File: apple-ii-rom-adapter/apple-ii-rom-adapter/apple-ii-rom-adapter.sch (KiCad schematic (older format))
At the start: 11 parts, among them J1 ROMSEL, J2 9316 insert, J3 74LS138 insert, U1 28C256, U2 74LS00, U3 74LS138

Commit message: Incremental update! Maybe this'll work? :-)
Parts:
- C1, C2, C3: footprint Capacitor_THT:CP_Radial_D6.3mm_P2.50mm -> Capacitor_THT:C_Disc_D5.0mm_W2.5mm_P5.00mm
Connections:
- net VCC: now also R2.1
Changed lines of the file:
@@
 F 0 "C1" H 6442 5646 50  0000 L CNN
 F 1 "0.1uF" H 6442 5555 50  0000 L CNN
-F 2 "Capacitor_THT:CP_Radial_D6.3mm_P2.50mm" H 6350 5600 50  0001 C CNN
+F 2 "Capacitor_THT:C_Disc_D5.0mm_W2.5mm_P5.00mm" H 6350 5600 50  0001 C CNN
 F 3 "~" H 6350 5600 50  0001 C CNN
 	1    6350 5600
@@
 F 0 "C2" H 7092 5646 50  0000 L CNN
 F 1 "0.1uF" H 7092 5555 50  0000 L CNN
-F 2 "Capacitor_THT:CP_Radial_D6.3mm_P2.50mm" H 7000 5600 50  0001 C CNN
+F 2 "Capacitor_THT:C_Disc_D5.0mm_W2.5mm_P5.00mm" H 7000 5600 50  0001 C CNN
 F 3 "~" H 7000 5600 50  0001 C CNN
 	1    7000 5600
@@
 F 0 "C3" H 7692 5646 50  0000 L CNN
 F 1 "0.1uF" H 7692 5555 50  0000 L CNN
-F 2 "Capacitor_THT:CP_Radial_D6.3mm_P2.50mm" H 7600 5600 50  0001 C CNN
+F 2 "Capacitor_THT:C_Disc_D5.0mm_W2.5mm_P5.00mm" H 7600 5600 50  0001 C CNN
 F 3 "~" H 7600 5600 50  0001 C CNN
 	1    7600 5600
@@
 $EndComp
 $Comp
-L power:GND #PWR?
+L power:GND #PWR0113
 U 1 1 60D30BF8
 P 6350 5700
-F 0 "#PWR?" H 6350 5450 50  0001 C CNN
+F 0 "#PWR0113" H 6350 5450 50  0001 C CNN
 F 1 "GND" H 6355 5527 50  0000 C CNN
 F 2 "" H 6350 5700 50  0001 C CNN
@@
 $EndComp
 $Comp
-L power:GND #PWR?
+L power:GND #PWR0114
 U 1 1 60D3171D
 P 7000 5700
-F 0 "#PWR?" H 7000 5450 50  0001 C CNN
+F 0 "#PWR0114" H 7000 5450 50  0001 C CNN
 F 1 "GND" H 7005 5527 50  0000 C CNN
 F 2 "" H 7000 5700 50  0001 C CNN
@@
 $EndComp
 $Comp
-L power:GND #PWR?
+L power:GND #PWR0115
 U 1 1 60D32097
 P 7600 5700
-F 0 "#PWR?" H 7600 5450 50  0001 C CNN
+F 0 "#PWR0115" H 7600 5450 50  0001 C CNN
 F 1 "GND" H 7605 5527 50  0000 C CNN
 F 2 "" H 7600 5700 50  0001 C CNN
@@
 $EndComp
 $Comp
-L power:VCC #PWR?
+L power:VCC #PWR0116
 U 1 1 60D32EAF
 P 6350 5500
-F 0 "#PWR?" H 6350 5350 50  0001 C CNN
+F 0 "#PWR0116" H 6350 5350 50  0001 C CNN
 F 1 "VCC" H 6365 5673 50  0000 C CNN
 F 2 "" H 6350 5500 50  0001 C CNN
@@
 $EndComp
 $Comp
-L power:VCC #PWR?
+L power:VCC #PWR0117
 U 1 1 60D33866
 P 7000 5500
-F 0 "#PWR?" H 7000 5350 50  0001 C CNN
+F 0 "#PWR0117" H 7000 5350 50  0001 C CNN
 F 1 "VCC" H 7015 5673 50  0000 C CNN
 F 2 "" H 7000 5500 50  0001 C CNN
@@
 $EndComp
 $Comp
-L power:VCC #PWR?
+L power:VCC #PWR0118
 U 1 1 60D346E6
 P 7600 5500
-F 0 "#PWR?" H 7600 5350 50  0001 C CNN
+F 0 "#PWR0118" H 7600 5350 50  0001 C CNN
 F 1 "VCC" H 7615 5673 50  0000 C CNN
 F 2 "" H 7600 5500 50  0001 C CNN
@@
 	1    0    0    -1
 $EndComp
+$Comp
+L power:VCC #PWR?
+U 1 1 60C6FC7E
+P 4250 5250
+F 0 "#PWR?" H 4250 5100 50  0001 C CNN
+F 1 "VCC" H 4265 5423 50  0000 C CNN
+F 2 "" H 4250 5250 50  0001 C CNN
+F 3 "" H 4250 5250 50  0001 C CNN
+	1    4250 5250
+	1    0    0    -1
+$EndComp

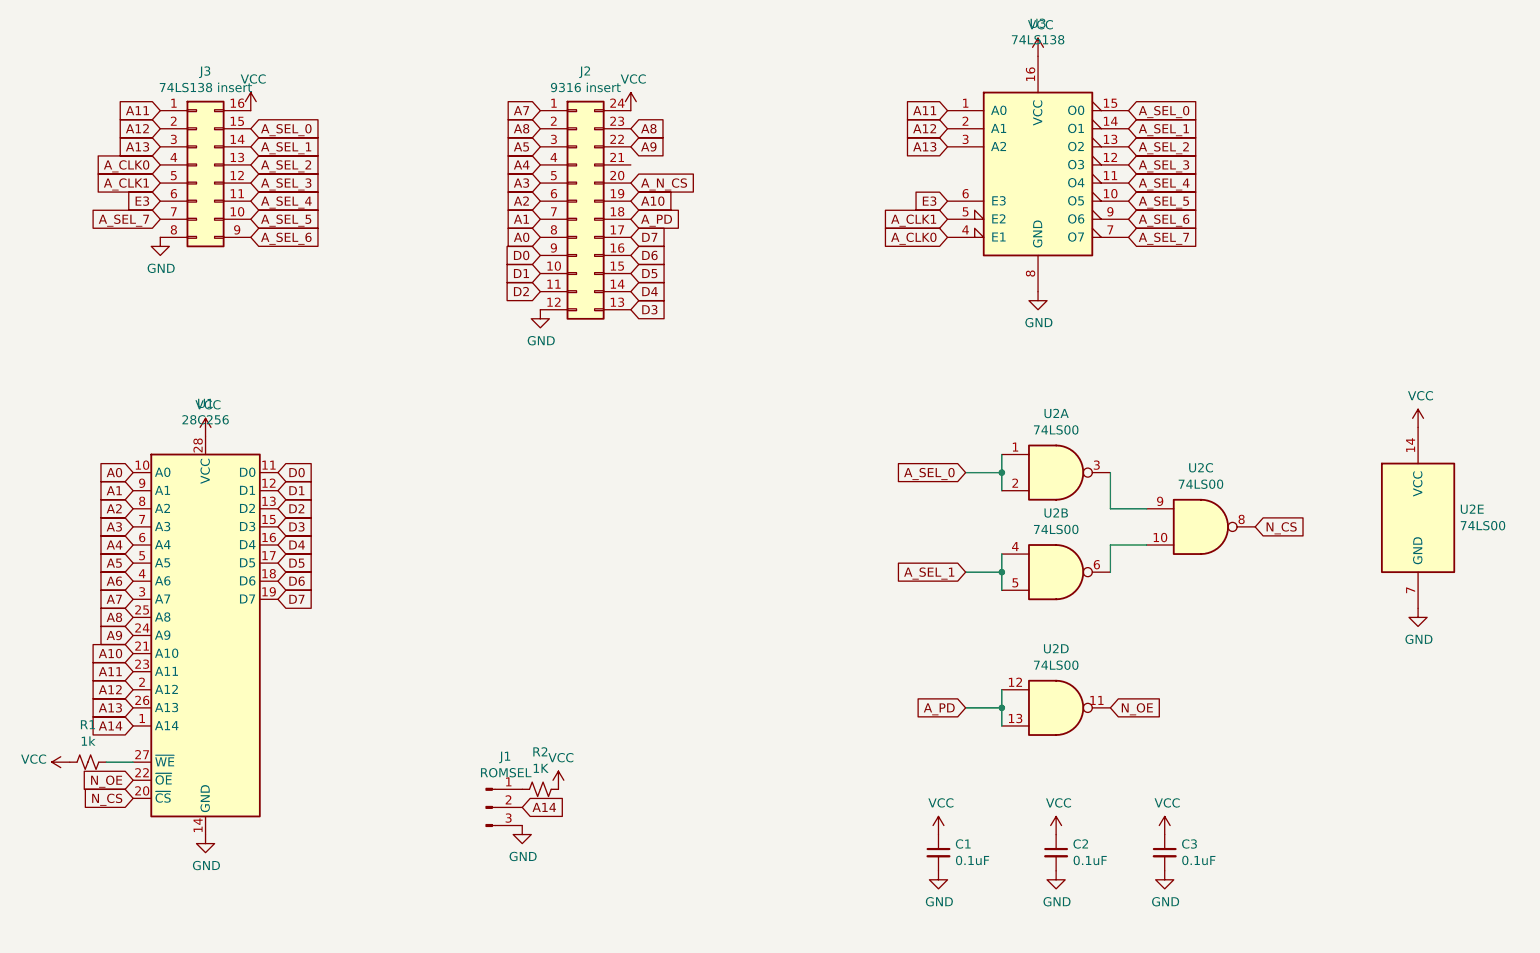
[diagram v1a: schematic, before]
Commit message: Updates to actually make this work!
It didn't work with this plugged in, ROM or not populated.

* Wow, I screwed up the address line naming, whoops, that removes a short
  across two address lines so now the apple-ii will boot with this plugged
  in w/ the 74LS138 populated but ROMs in the normal ROM slots.

* Wow, I fucked up the logic.  The logic I chose plainly wouldn't work.
  Replace it with a pair of NAND gates and a NOR gate to implement the
  correct /CS logic.  This now boots to integer basic.

Tested:

* integer basic image with original non autostart monitor - E000G jumps
  to integer BASIC fine.

* integer basic image with language card installed - the autostart
  monitor does indeed jump to integer basic AND this demonstrates the
  inhibit line logic works fine.

Aiee, etc.
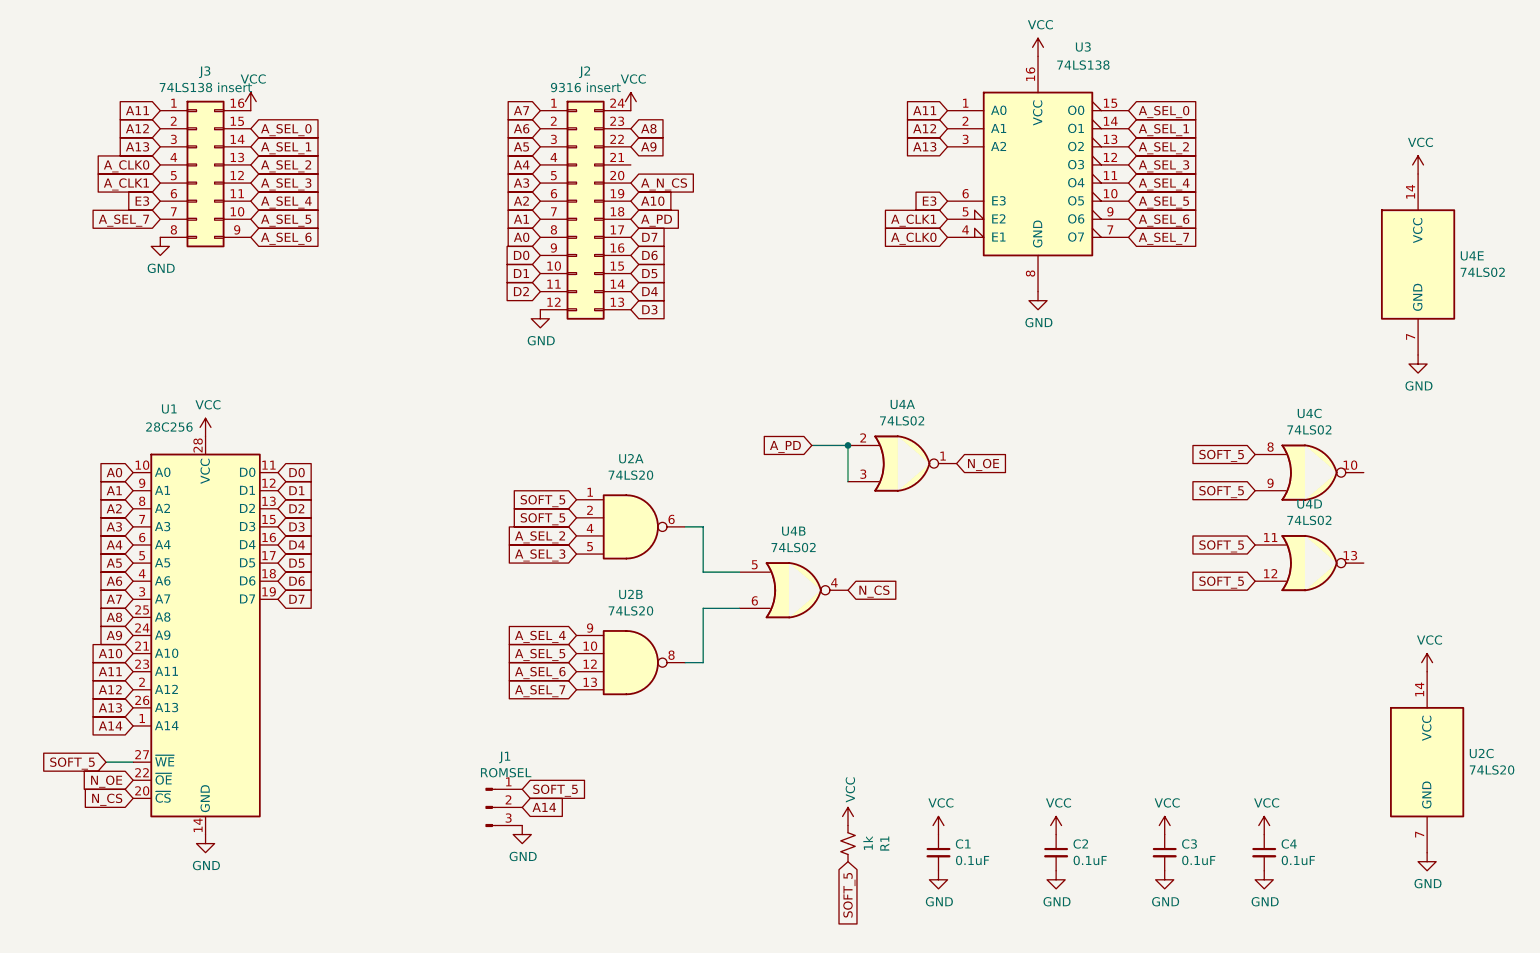
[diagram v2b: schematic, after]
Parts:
- removed R2: 1K, Resistor_THT:R_Axial_DIN0309_L9.0mm_D3.2mm_P15.24mm_Horizontal, symbol Device:R_Small_US
- removed U2: 74LS00, Package_DIP:DIP-14_W7.62mm_Socket, symbol 74xx:74LS00
- added C4: 0.1uF, Capacitor_THT:C_Disc_D5.0mm_W2.5mm_P5.00mm, symbol Device:C_Small
- added U2: 74LS20, Package_DIP:DIP-14_W7.62mm_Socket, symbol 74xx:74LS20
- added U4: 74LS02, Package_DIP:DIP-14_W7.62mm_Socket, symbol 74xx:74LS02
- R1: footprint Resistor_THT:R_Axial_DIN0309_L9.0mm_D3.2mm_P15.24mm_Horizontal -> Resistor_THT:R_Axial_DIN0207_L6.3mm_D2.5mm_P7.62mm_Horizontal
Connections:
- net A6: now also J2.2 (Pin_2)
- net A8: no longer J2.2 (Pin_2)
- net A_PD: now also U4.2, U4.3
- net A_SEL_2: now also U2.4
- net A_SEL_3: now also U2.5
- net A_SEL_4: now also U2.9
- net A_SEL_5: now also U2.10
- net A_SEL_6: now also U2.12
- net A_SEL_7: now also U2.13
- net GND: now also C4.2, U2.7 (GND), U4.7 (GND)
- net N_CS: now also U4.4
- net N_OE: now also U4.1
- net VCC: now also C4.1, U2.14 (VCC), U4.14 (VCC)
- net SOFT_5: now reaches R1.1, U1.27 (~WE)
- net SOFT_5: now also J1.1 (Pin_1), U2.1, U2.2, U4.11, U4.12, U4.8, U4.9
- new net: U2.6, U4.5
- new net: U2.8, U4.6
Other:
- moved on the sheet: R1
